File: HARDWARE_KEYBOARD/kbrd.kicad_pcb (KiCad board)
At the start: 2 copper layers, 70 x 50 mm, 24 parts, among them J1 USB_C_Receptacle_USB2.0_16P, J2 SWD, SW1 SW_SPST, SW2 SW_SPST, SW3 SW_SPST, SW4 SW_SPST, U1 STM32F103C8Tx, U2 AP2210N-3.3TRG1, Y1 Crystal_GND24

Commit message: Updated PCB & schematic
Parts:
- J2: footprint Connector_PinHeader_2.54mm:PinHeader_1x04_P2.54mm_Vertical -> Connector_PinHeader_2.00mm:PinHeader_1x04_P2.00mm_Vertical
- Y1: footprint Oscillator:Oscillator_SMD_Abracon_ASE-4Pin_3.2x2.5mm -> Oscillator:Oscillator_SMD_Abracon_ASV-4Pin_7.0x5.1mm
- moved J2 21.1 mm to (125.6, 90.8), turned to 180 degrees
- moved C1 18.8 mm to (142.4, 79.2), turned to 0 degrees
- moved C4 17.6 mm to (142.6, 88.4)
- moved C5 17.6 mm to (142.6, 91.7)
- moved C3 17.5 mm to (142.6, 85.2)
- moved C2 17.3 mm to (142.4, 75.8), turned to 0 degrees
- moved Y1 15.4 mm to (135.1, 77.2)
- moved C6 10.9 mm to (170.8, 90.9), turned to 90 degrees
- moved R1 8.80 mm to (177.3, 85.8), turned to 180 degrees
- moved U1 5.59 mm to (133.8, 88.0), turned to 0 degrees
- moved U2 4.74 mm to (175.4, 90.8), turned to 180 degrees
- moved R3 3.47 mm to (167.5, 90.0)
- moved R2 3.23 mm to (172.6, 85.8), turned to 180 degrees
- moved D5 2.94 mm to (167.6, 85.8), turned to 0 degrees
- moved D1 2.50 mm to (163.3, 79.5)
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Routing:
- net +3.3V: track 0.00 -> 92.7 mm
- net GND: track 0.00 -> 81.8 mm, vias 0 -> 7
- net /COL2: track 0.00 -> 57.5 mm, vias 0 -> 3
- net /COL3: track 0.00 -> 57.3 mm
- net /ROW2: track 0.00 -> 51.7 mm, vias 0 -> 1
- net /PA11: track 0.00 -> 46.0 mm, vias 0 -> 2
- net /PA12: track 0.00 -> 45.8 mm, vias 0 -> 3
- net /ROW1: track 0.00 -> 33.5 mm, vias 0 -> 2
- net /OSC_OUT: track 0.00 -> 27.4 mm, vias 0 -> 2
- net /OSC_IN: track 0.00 -> 21.5 mm, vias 0 -> 2
- net /COL1: track 0.00 -> 19.9 mm
- net /SWDIO: track 0.00 -> 18.3 mm, vias 0 -> 1
- net /SWCLK: track 0.00 -> 15.4 mm, vias 0 -> 1
- net Net-(D5-A): track 0.00 -> 13.9 mm
- net VCC: track 0.00 -> 11.1 mm
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- added copper zone on B.Cu, net GND
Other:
- board size 70 x 50 mm -> 65 x 46.5 mm

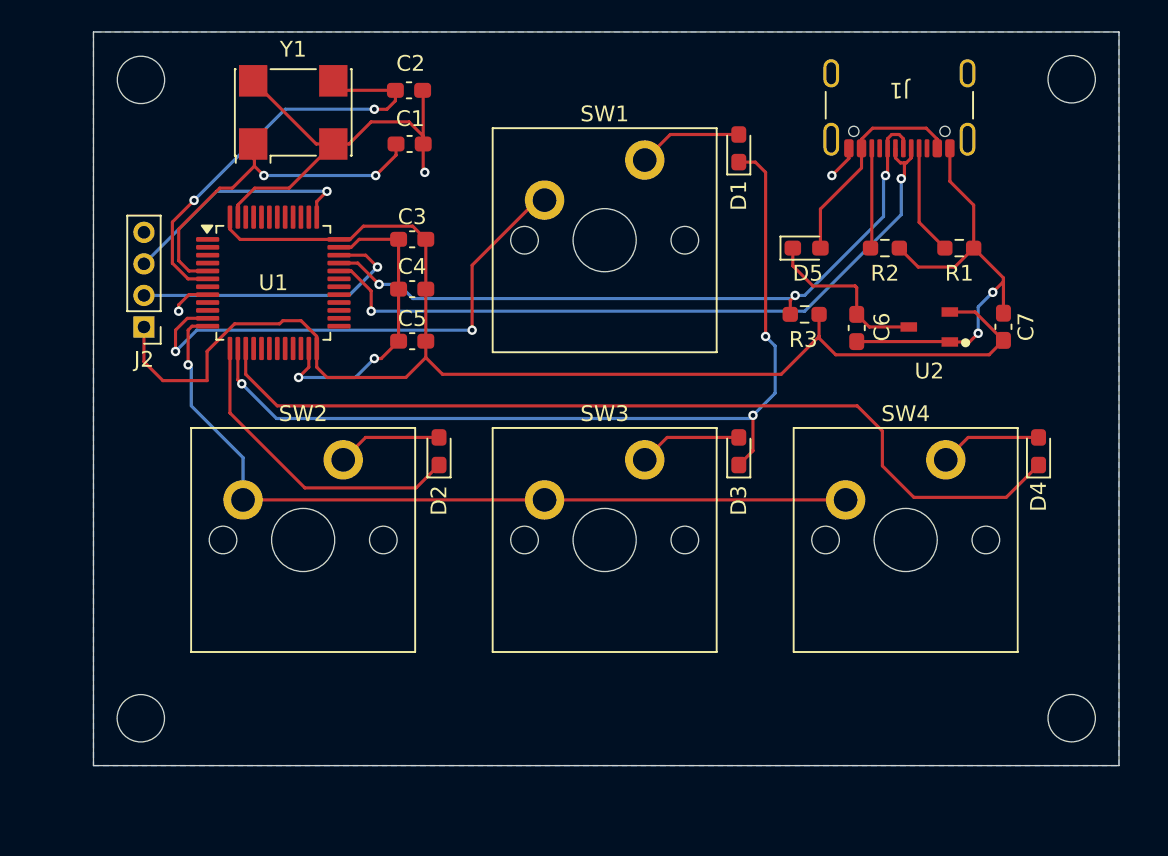
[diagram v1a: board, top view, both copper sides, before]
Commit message: Add copper zones; remove extra GND traces
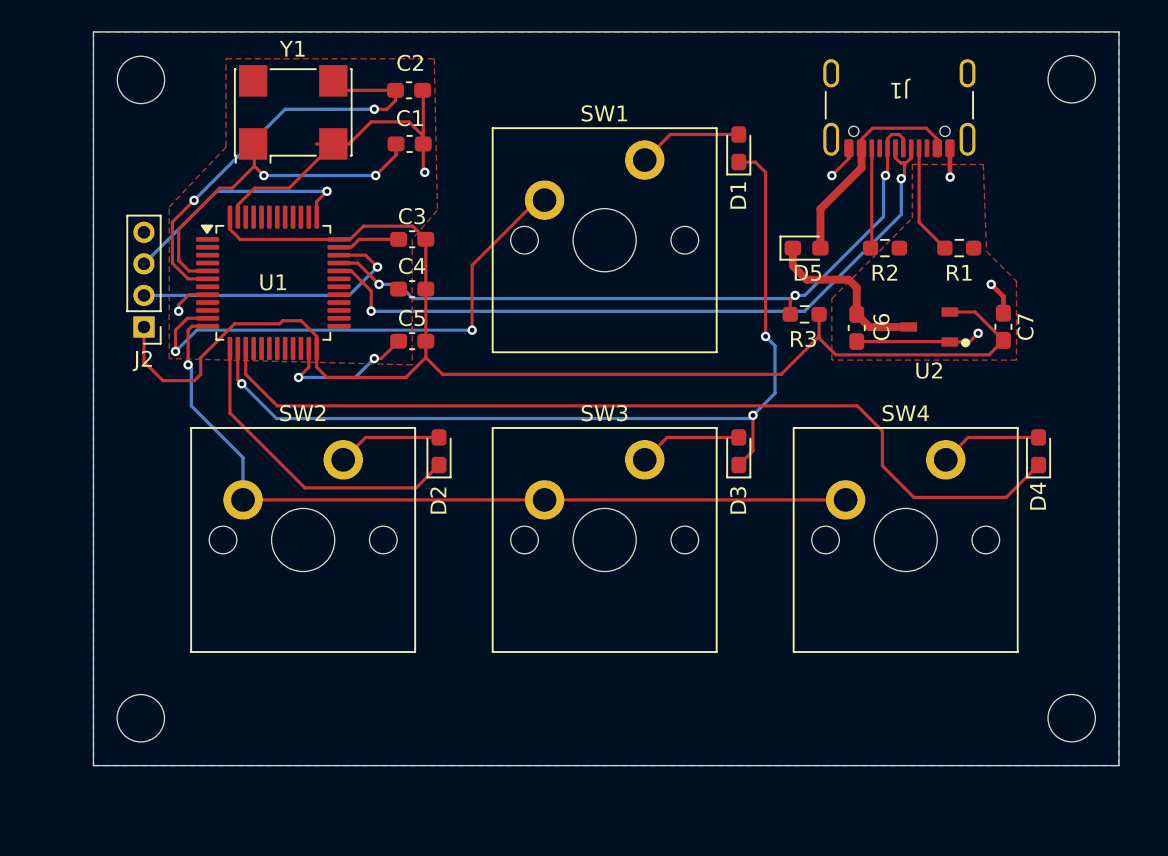
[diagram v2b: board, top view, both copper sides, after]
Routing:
- net GND: track 81.8 -> 52.0 mm, vias 7 -> 8
- added copper zone on F.Cu, net GND

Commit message: Add gerber
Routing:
- net GND: track 52.0 -> 30.6 mm
- net +3.3V: track 92.2 -> 95.6 mm
- net /OSC_IN: track 21.5 -> 22.7 mm
- net /COL2: track 57.5 -> 58.5 mm
- net /COL1: track 19.9 -> 20.7 mm
- net /ROW1: track 33.5 -> 34.3 mm
- net /OSC_OUT: track 27.4 -> 28.2 mm
- net /PA12: track 45.8 -> 46.4 mm
- net /SWDIO: track 18.3 -> 18.8 mm

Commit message: Chane volt regulator footprint to fit the one im going to use
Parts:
- U2: footprint AP2210N-3.3TRG1:SOT95P280X145-3N -> Package_TO_SOT_SMD:SOT-23-3
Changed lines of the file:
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@@
 		)
 	)
-	(footprint "AP2210N-3.3TRG1:SOT95P280X145-3N"
+	(footprint "Package_TO_SOT_SMD:SOT-23-3"
 		(layer "F.Cu")
 		(at 175.375 90.8 180)
+		(descr "SOT, 3 Pin (https://www.jedec.org/sites/default/files/docs/Mo-178D.PDF inferred 3-pin variant), generated with kicad-footprint-generator ipc_gullwing_generator.py")
+		(tags "SOT TO_SOT_SMD")
 		(property "Reference" "U2"
-			(at 0 -2.8 0)
-			(layer "F.SilkS")
-			(effects
-				(font
-					(size 1.000638 1.000638)
+			(at 0 -2.4 180)
+			(layer "F.SilkS")
+			(effects
+				(font
+					(size 1 1)
 					(thickness 0.15)
 				)
@@
 		)
 		(property "Value" "AP2210N-3.3TRG1"
-			(at 8.2241 2.46923 0)
-			(layer "F.Fab")
-			(hide yes)
-			(effects
-				(font
-					(size 1.001717 1.001717)
-					(thickness 0.15)
-				)
-			)
-		)
-		(property "Footprint" "AP2210N-3.3TRG1:SOT95P280X145-3N"
-			(at 0 0 0)
+			(at 0 2.4 180)
+			(layer "F.Fab")
+			(hide yes)
+			(effects
+				(font
+					(size 1 1)
+					(thickness 0.15)
+				)
+			)
+		)
+		(property "Footprint" "Package_TO_SOT_SMD:SOT-23-3"
+			(at 0 0 180)
+			(unlocked yes)
 			(layer "F.Fab")
 			(hide yes)
@@
 		)
 		(property "Datasheet" ""
-			(at 0 0 0)
+			(at 0 0 180)
+			(unlocked yes)
 			(layer "F.Fab")
 			(hide yes)
@@
 		)
 		(property "Description" ""
-			(at 0 0 0)
+			(at 0 0 180)
+			(unlocked yes)
 			(layer "F.Fab")
 			(hide yes)
@@
 		(sheetfile "kbrd.kicad_sch")
 		(attr smd)
-		(fp_circle
-			(center -2.3 -1)
-			(end -2.076394 -1)
-			(stroke
-				(width 0.127)
-				(type solid)
-			)
-			(fill none)
-			(layer "F.SilkS")
-		)
-		(fp_circle
-			(center -2.3 -1)
-			(end -2.158581 -1)
-			(stroke
-				(width 0.127)
-				(type solid)
-			)
-			(fill none)
-			(layer "F.SilkS")
-		)
-		(fp_circle
-			(center -2.3 -1)
-			(end -2.2 -1)
-			(stroke
-				(width 0.127)
-				(type solid)
-			)
-			(fill none)
-			(layer "F.SilkS")
-		)
-		(fp_circle
-			(center -2.4 -1)
-			(end -2.3 -1)
-			(stroke
-				(width 0.127)
-				(type solid)
-			)
-			(fill none)
-			(layer "F.SilkS")
-		)
-		(fp_line
-			(start 2.1 1.8)
-			(end -2.1 1.8)
+		(fp_line
+			(start 0 1.56)
+			(end 0.8 1.56)
+			(stroke
+				(width 0.12)
+				(type solid)
+			)
+			(layer "F.SilkS")
+		)
+		(fp_line
+			(start 0 1.56)
+			(end -0.8 1.56)
+			(stroke
+				(width 0.12)
+				(type solid)
+			)
+			(layer "F.SilkS")
+		)
+		(fp_line
+			(start 0 -1.56)
+			(end 0.8 -1.56)
+			(stroke
+				(width 0.12)
+				(type solid)
+			)
+			(layer "F.SilkS")
+		)
+		(fp_line
+			(start 0 -1.56)
+			(end -0.8 -1.56)
+			(stroke
+				(width 0.12)
+				(type solid)
+			)
+			(layer "F.SilkS")
+		)
+		(fp_poly
+			(pts
+				(xy -1.3 -1.51) (xy -1.54 -1.84) (xy -1.06 -1.84) (xy -1.3 -1.51)
+			)
+			(stroke
+				(width 0.12)
+				(type solid)
+			)
+			(fill solid)
+			(layer "F.SilkS")
+		)
+		(fp_line
+			(start 2.05 1.7)
+			(end 2.05 -1.7)
 			(stroke
 				(width 0.05)
@@
 		)
 		(fp_line
-			(start 2.1 -1.8)
-			(end 2.1 1.8)
+			(start 2.05 -1.7)
+			(end -2.05 -1.7)
 			(stroke
 				(width 0.05)
@@
 		)
 		(fp_line
-			(start -2.1 1.8)
-			(end -2.1 -1.8)
+			(start -2.05 1.7)
+			(end 2.05 1.7)
 			(stroke
 				(width 0.05)
@@
 		)
 		(fp_line
-			(start -2.1 -1.8)
-			(end 2.1 -1.8)
+			(start -2.05 -1.7)
+			(end -2.05 1.7)
 			(stroke
 				(width 0.05)
@@
 			(layer "F.CrtYd")
 		)
-		(pad "1" smd rect
-			(at -1.3 -0.95 180)
-			(size 1.05 0.6)
+		(fp_line
+			(start 0.8 1.45)
+			(end -0.8 1.45)
+			(stroke
+				(width 0.1)
+				(type solid)
+			)
+			(layer "F.Fab")
+		)
+		(fp_line
+			(start 0.8 -1.45)
+			(end 0.8 1.45)
+			(stroke
+				(width 0.1)
+				(type solid)
+			)
+			(layer "F.Fab")
+		)
+		(fp_line
+			(start -0.4 -1.45)
+			(end 0.8 -1.45)
+			(stroke
+				(width 0.1)
+				(type solid)
+			)
+			(layer "F.Fab")
+		)
+		(fp_line
+			(start -0.8 1.45)
+			(end -0.8 -1.05)
+			(stroke
+				(width 0.1)
+				(type solid)
+			)
+			(layer "F.Fab")
+		)
+		(fp_line
+			(start -0.8 -1.05)
+			(end -0.4 -1.45)
+			(stroke
+				(width 0.1)
+				(type solid)
+			)
+			(layer "F.Fab")
+		)
+		(fp_text user "${REFERENCE}"
+			(at 0 0 180)
+			(layer "F.Fab")
+			(effects
+				(font
+					(size 0.4 0.4)
+					(thickness 0.06)
+				)
+			)
+		)
+		(pad "1" smd roundrect
+			(at -1.1375 -0.95 180)
+			(size 1.325 0.6)
 			(layers "F.Cu" "F.Paste" "F.Mask")
+			(roundrect_rratio 0.25)
 			(net 47 "GND")
 			(pinfunction "GND")
 			(pintype "power_in")
-			(solder_mask_margin 0.102)
-		)
-		(pad "2" smd rect
-			(at -1.3 0.95 180)
-			(size 1.05 0.6)
+		)
+		(pad "2" smd roundrect
+			(at -1.1375 0.95 180)
+			(size 1.325 0.6)
 			(layers "F.Cu" "F.Paste" "F.Mask")
+			(roundrect_rratio 0.25)
 			(net 57 "+3.3V")
 			(pinfunction "VOUT")
 			(pintype "output")
-			(solder_mask_margin 0.102)
-		)
-		(pad "3" smd rect
-			(at 1.3 0 180)
-			(size 1.05 0.6)
+		)
+		(pad "3" smd roundrect
+			(at 1.1375 0 180)
+			(size 1.325 0.6)
 			(layers "F.Cu" "F.Paste" "F.Mask")
+			(roundrect_rratio 0.25)
 			(net 17 "VCC")
 			(pinfunction "VIN")
 			(pintype "input")
-			(solder_mask_margin 0.102)
-		)
-		(model "${MY}/AP2210N-3.3TRG1/AP2210N-3.3TRG1.step"
+		)
+		(model "${KICAD8_3DMODEL_DIR}/Package_TO_SOT_SMD.3dshapes/SOT-23-3.wrl"
 			(offset
 				(xyz 0 0 0)
@@
 			)
 			(rotate
-				(xyz -90 0 0)
-			)
-		)
+				(xyz 0 0 0)
+			)
+		)
